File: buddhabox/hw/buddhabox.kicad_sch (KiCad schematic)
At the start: 52 parts, among them J1 Serial, J2 SWD, J3 USB_B_Micro, J4 Speaker, J5 Battery, SW1 SW_Push, SW3 SW_Push, SW4 SW_Push, U1 TPS61291DRVR, U3 RP2040, U4 PAM8302AAD, U5 W25Q32JVZPIQ, Y1 Crystal_4pin_SMD

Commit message: Updated with working board design and pictures.
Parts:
- removed D2: LED Red, LED_SMD:LED_0603_1608Metric, symbol Device:LED_Small
- removed R5: 1k, Resistor_SMD:R_0402_1005Metric, symbol Device:R
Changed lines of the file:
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@@
-    (stroke (width 0) (type default) (color 0 0 0 0))
-  )
-  (wire (pts (xy 151.13 30.48) (xy 151.13 33.02))
     (stroke (width 0) (type default) (color 0 0 0 0))
   )
@@
     (stroke (width 0) (type default) (color 0 0 0 0))
   )
-  (wire (pts (xy 151.13 38.1) (xy 151.13 39.37))
-    (stroke (width 0) (type default) (color 0 0 0 0))
-  )
   (wire (pts (xy 166.37 124.46) (xy 166.37 137.16))
     (stroke (width 0) (type default) (color 0 0 0 0))
@@
     (stroke (width 0) (type default) (color 0 0 0 0))
   )
-  (wire (pts (xy 148.59 30.48) (xy 151.13 30.48))
-    (stroke (width 0) (type default) (color 0 0 0 0))
-  )
   (wire (pts (xy 248.92 31.75) (xy 257.81 31.75))
     (stroke (width 0) (type default) (color 0 0 0 0))
@@
   )
   (wire (pts (xy 86.36 165.1) (xy 78.74 165.1))
-    (stroke (width 0) (type default) (color 0 0 0 0))
-  )
-  (wire (pts (xy 138.43 30.48) (xy 140.97 30.48))
     (stroke (width 0) (type default) (color 0 0 0 0))
   )
@@
       (effects (font (size 1.27 1.27)) hide)
     )
-    (pin "1")
-    (pin "2")
-  )
-  (symbol (lib_id "Device:R") (at 144.78 30.48 90) (unit 1)
-    (in_bom yes) (on_board yes)
-    (property "Reference" "R5" (id 0) (at 144.78 28.448 90))
-    (property "Value" "1k" (id 1) (at 144.78 30.48 90))
-    (property "Footprint" "Resistor_SMD:R_0402_1005Metric" (id 2) (at 144.78 32.258 0)
-      (effects (font (size 1.27 1.27)) hide)
-    )
-    (property "Datasheet" "" (id 3) (at 144.78 30.48 0))
     (pin "1")
     (pin "2")
@@
     (pin "1")
   )
-  (symbol (lib_id "Device:LED_Small") (at 151.13 35.56 90) (unit 1)
-    (in_bom yes) (on_board yes)
-    (property "Reference" "D2" (id 0) (at 152.908 34.3916 90)
-      (effects (font (size 1.27 1.27)) (justify right))
-    )
-    (property "Value" "LED Red" (id 1) (at 152.908 36.703 90)
-      (effects (font (size 1.27 1.27)) (justify right))
-    )
-    (property "Footprint" "LED_SMD:LED_0603_1608Metric" (id 2) (at 151.13 35.56 90)
-      (effects (font (size 1.27 1.27)) hide)
-    )
-    (property "Datasheet" "~" (id 3) (at 151.13 35.56 90)
-      (effects (font (size 1.27 1.27)) hide)
-    )
-    (pin "1")
-    (pin "2")
-  )
   (symbol (lib_id "power:GND") (at 25.4 134.62 0) (unit 1)
     (in_bom yes) (on_board yes)
@@
     (pin "1")
     (pin "2")
-  )
-  (symbol (lib_id "power:GND") (at 151.13 39.37 0) (unit 1)
-    (in_bom yes) (on_board yes)
-    (property "Reference" "#PWR012" (id 0) (at 151.13 45.72 0)
-      (effects (font (size 1.27 1.27)) hide)
-    )
-    (property "Value" "GND" (id 1) (at 151.13 43.18 0))
-    (property "Footprint" "" (id 2) (at 151.13 39.37 0))
-    (property "Datasheet" "" (id 3) (at 151.13 39.37 0))
-    (pin "1")
   )
   (symbol (lib_id "Switch:SW_Push") (at 17.78 118.11 270) (unit 1)
@@
       (reference "#PWR010") (unit 1) (value "GND") (footprint "")
     )
-    (path "/cf630c1e-095e-4ed8-96bd-413e1bdb3133"
-      (reference "#PWR012") (unit 1) (value "GND") (footprint "")
-    )
     (path "/4dd818ac-3292-4a28-a1e2-f99034e0b642"
       (reference "#PWR013") (unit 1) (value "+1V1") (footprint "")
@@
       (reference "D1") (unit 1) (value "BAT54C") (footprint "Package_TO_SOT_SMD:SOT-23")
     )
-    (path "/85bc6096-6810-4070-a31a-8493abed0b37"
-      (reference "D2") (unit 1) (value "LED Red") (footprint "LED_SMD:LED_0603_1608Metric")
-    )
     (path "/abe3b920-b697-4d1e-85f2-265143b11672"
       (reference "D3") (unit 1) (value "LED Green") (footprint "LED_SMD:LED_0603_1608Metric")
@@
       (reference "R2") (unit 1) (value "1k") (footprint "Resistor_SMD:R_0402_1005Metric")
     )
-    (path "/1e216b41-6f2d-4dc7-be4b-6f214a082fa7"
-      (reference "R5") (unit 1) (value "1k") (footprint "Resistor_SMD:R_0402_1005Metric")
-    )
     (path "/c1d41f5e-3500-4d8b-aba5-66d1af96b463"

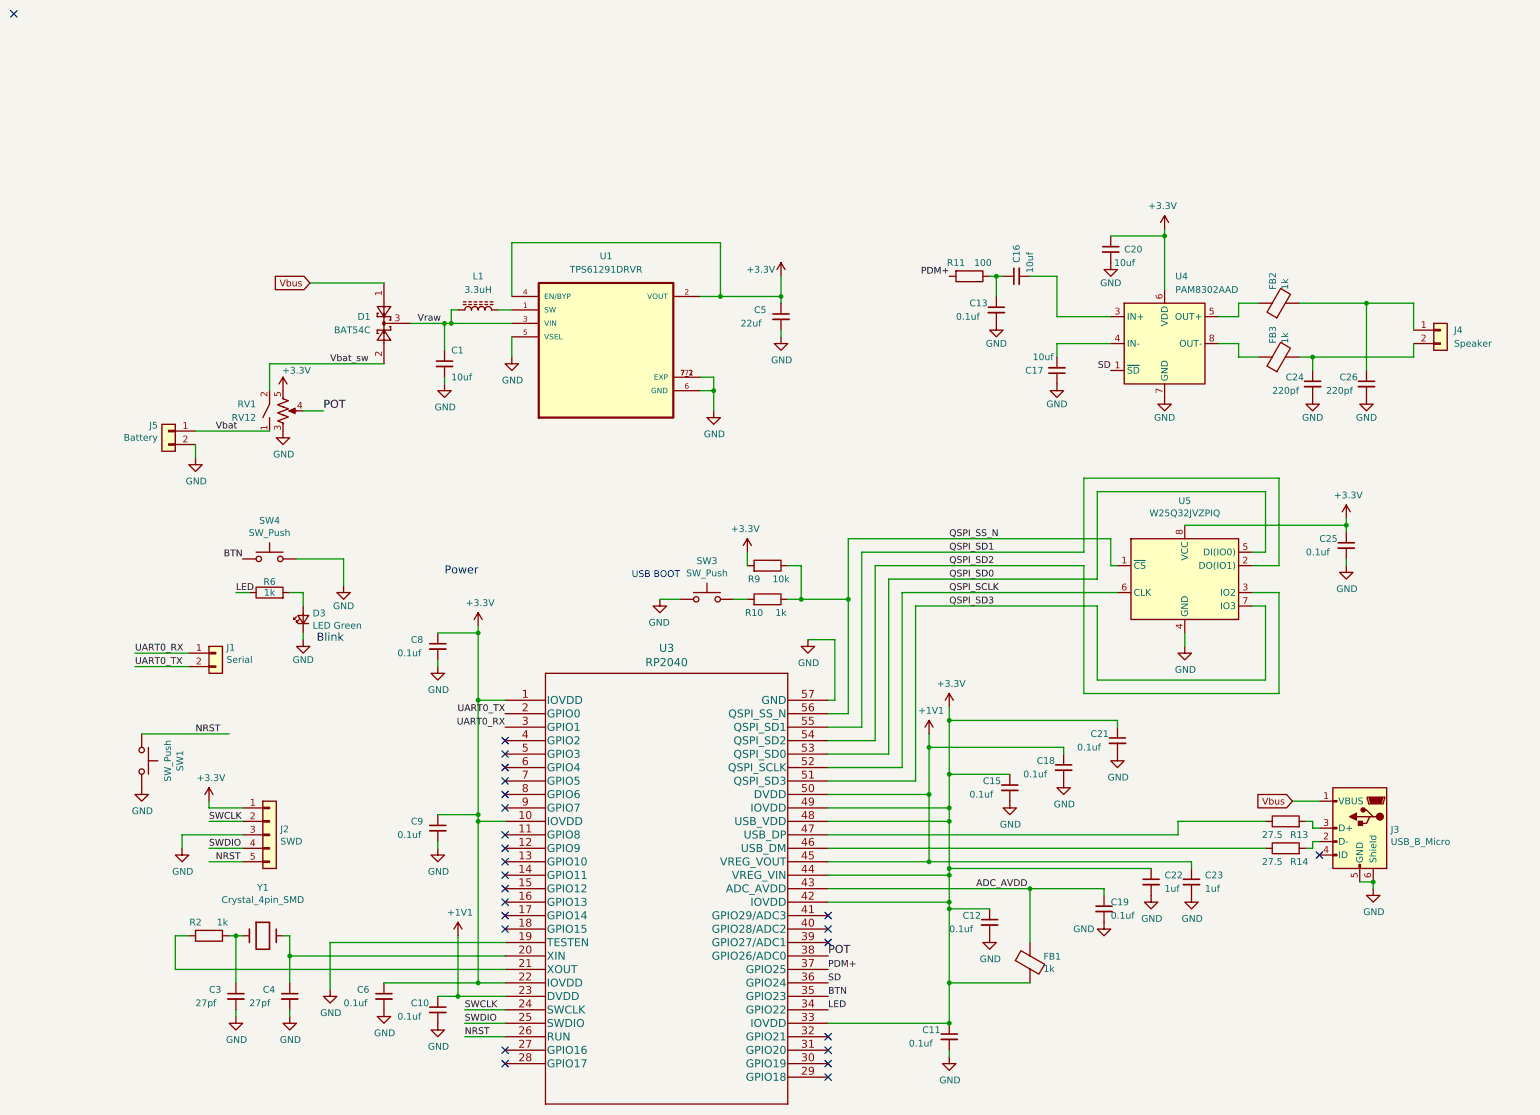
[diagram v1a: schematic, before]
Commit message: switch to i2s amp & added LDO to vbus
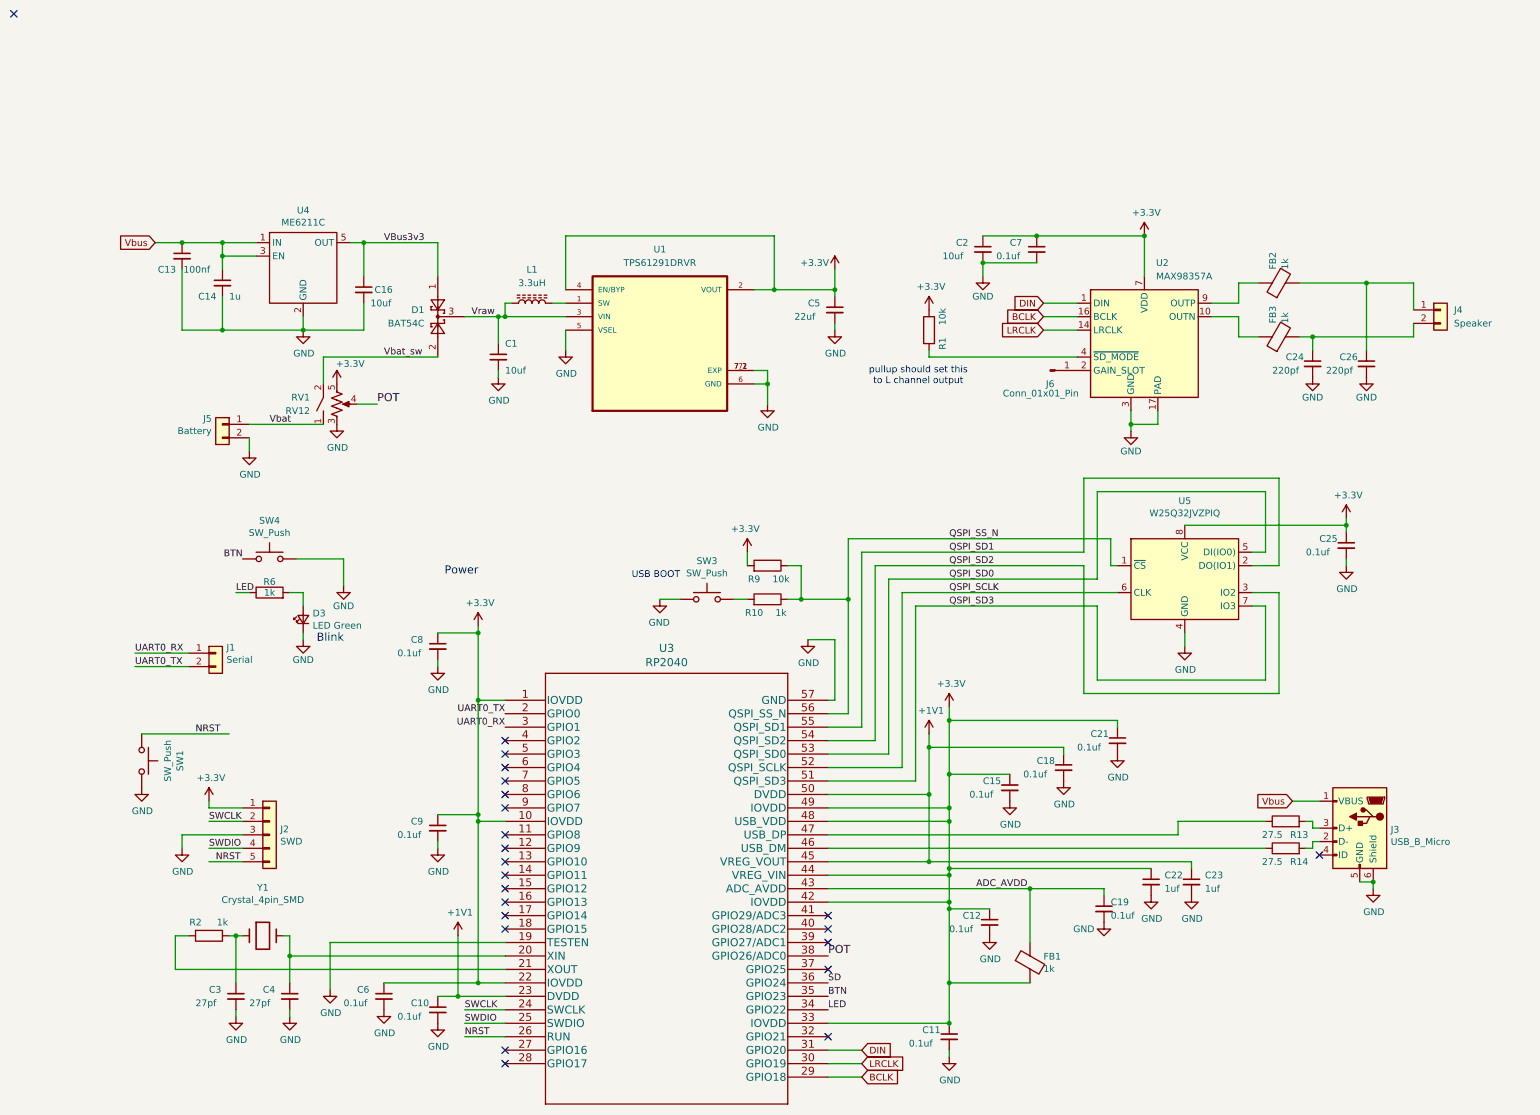
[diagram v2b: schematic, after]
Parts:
- removed C17, C20: 10uf, Capacitor_SMD:C_0805_2012Metric, symbol Device:C_Small
- removed R11: 100, Resistor_SMD:R_0402_1005Metric, symbol Device:R
- removed U4: PAM8302AAD, Package_SO:TSSOP-8_3x3mm_P0.65mm, symbol Amplifier_Audio:PAM8302AAD
- added C14: 1u, Capacitor_SMD:C_0402_1005Metric, symbol Device:C_Small
- added C2: 10uf, Capacitor_SMD:C_0402_1005Metric, symbol Device:C_Small
- added C7: 0.1uf, Capacitor_SMD:C_0402_1005Metric, symbol Device:C_Small
- added J6: Conn_01x01_Pin, symbol Connector:Conn_01x01_Pin
- added R1: 10k, Resistor_SMD:R_0402_1005Metric, symbol Device:R
- added U2: MAX98357A, Package_DFN_QFN:TQFN-16-1EP_3x3mm_P0.5mm_EP1.23x1.23mm, symbol Audio:MAX98357A
- added U4: ME6211C, Package_TO_SOT_SMD:SOT-23-5, symbol buddabox_lib:ME6211C
- C13: value 0.1uf -> 100nf
- C16: footprint Capacitor_SMD:C_0805_2012Metric -> Capacitor_SMD:C_0402_1005Metric
- U3: LCSC (none) -> C2040
- U5: LCSC (none) -> C571260
- Y1: LCSC (none) -> C9002
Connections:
- net +3.3V: now also C2.1, C7.1, R1.1, U2.7 (VDD), U2.8 (VDD)
- net GND: now also C16.2, C14.2, C2.2, C7.2, U2.11 (GND), U2.15 (GND), U2.17 (PAD), U2.3 (GND), U4.2 (GND)
- net Vbus: now also C13.1, C14.1, U4.1 (IN), U4.3 (EN); no longer D1.1
- net at FB3.1: now also U2.10 (OUTN)
- net VBus3v3: now reaches C16.1
- net VBus3v3: now also D1.1, U4.5 (OUT); no longer C13.1
- net at FB2.1: now also U2.9 (OUTP)
- net BCLK: now reaches U3.29 (GPIO18)
- net BCLK: now also U2.16 (BCLK)
- net LRCLK: now reaches U3.30 (GPIO19)
- net LRCLK: now also U2.14 (LRCLK)
- net DIN: now reaches U3.31 (GPIO20)
- net DIN: now also U2.1 (DIN)
- net PDM+: no longer names the net of U3.37 (GPIO25)
- new net: R1.2, U2.4 (~{SD_MODE})
- new net: J6.1 (Pin_1), U2.2 (GAIN_SLOT)
- no-connect marks 25 -> 23
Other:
- note added: "pullup should set this to L channel output"
- moved on the sheet: C1, C24, C26, C5, D1, FB2, FB3, J4, J5, L1, RV1, U1

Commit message: updated schematic with lcsc part numbers
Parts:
- removed C13: 100nf, Capacitor_SMD:C_0402_1005Metric, symbol Device:C_Small
- removed C14: 1u, Capacitor_SMD:C_0402_1005Metric, symbol Device:C_Small
- removed C16: 10uf, Capacitor_SMD:C_0402_1005Metric, symbol Device:C_Small
- removed J1: Serial, Connector_PinHeader_2.54mm:PinHeader_1x02_P2.54mm_Vertical, symbol Connector_Generic:Conn_01x02
- removed J3: USB_B_Micro, Connector_USB:USB_Micro-B_Amphenol_10103594-0001LF_Horizontal, symbol Connector:USB_B_Micro
- removed J6: Conn_01x01_Pin, symbol Connector:Conn_01x01_Pin
- removed L1: 3.3uH, Inductor_SMD:L_Taiyo-Yuden_MD-2020, symbol Device:L_Ferrite
- removed R13, R14: 27.5, Resistor_SMD:R_0402_1005Metric, symbol Device:R
- removed U1: TPS61291DRVR, emeb_library:SON65P200X200X80-7N, symbol emeb_library:TPS61291DRVR
- removed U4: ME6211C, Package_TO_SOT_SMD:SOT-23-5, symbol buddabox_lib:ME6211C
- added C17: 0.1uf, Capacitor_SMD:C_0402_1005Metric, symbol Device:C_Small
- added C20, C27: 10uf, Capacitor_SMD:C_0402_1005Metric, symbol Device:C_Small
- added J7: USB_C_Receptacle_USB2.0, MyLibrary:USB-C_SMD-TYPE-C-31-M-12, symbol Connector:USB_C_Receptacle_USB2.0
- added JP1: Jumper_2_Bridged, Jumper:SolderJumper-2_P1.3mm_Bridged_Pad1.0x1.5mm, symbol Jumper:Jumper_2_Bridged
- added L2: 1.5uH, Inductor_SMD:L_Coilcraft_LPS3010, symbol Device:L_Ferrite
- added R3, R4: 5.1k, Resistor_SMD:R_0402_1005Metric, symbol Device:R
- added R5, R7: 27.4, Resistor_SMD:R_0402_1005Metric, symbol Device:R
- added R8: 100k, Resistor_SMD:R_0805_2012Metric, symbol Device:R
- added U6: TPS63031DSK, Package_SON:WSON-10-1EP_2.5x2.5mm_P0.5mm_EP1.2x2mm, symbol Regulator_Switching:TPS63031DSK
- C1: footprint Capacitor_SMD:C_0805_2012Metric -> Capacitor_SMD:C_0402_1005Metric; LCSC (none) -> C15525
- C10, C11, C12, C15, C18, C19, C21, C25, C6, C7, C8, C9: LCSC (none) -> C1525
- C2: LCSC (none) -> C15525
- C22, C23: LCSC (none) -> C52923
- C24, C26: LCSC (none) -> C1530
- C3, C4: value 27pf -> 30pf; footprint Capacitor_SMD:C_0402_1005Metric -> Capacitor_SMD:C_0603_1608Metric; LCSC (none) -> C1658
- C5: value 22uf -> 10uf; footprint Capacitor_SMD:C_1210_3225Metric -> Capacitor_SMD:C_0402_1005Metric; LCSC (none) -> C15525
- D1: LCSC (none) -> C556168
- D3: LCSC (none) -> C2286
- FB1, FB2, FB3: value 1k -> 600@100mhz; footprint Inductor_SMD:L_0402_1005Metric -> Inductor_SMD:L_0603_1608Metric; LCSC (none) -> C1002
- J2: value SWD -> PICOPROBE
- R1, R9: LCSC (none) -> C25744
- R10, R2, R6: LCSC (none) -> C11702
- SW1, SW3: LCSC (none) -> C221675
- SW4: value SW_Push -> SW_PushSide; LCSC (none) -> DNP
- U2: LCSC (none) -> C910544
- U5: value W25Q32JVZPIQ -> W25Q64JVZPIQ; LCSC C571260 -> C2940197
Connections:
- net VBus3v3 is gone; now on net Vbus: D1.1
- net +3.3V: now also C20.1, C27.1, JP1.1 (A), U6.1 (VOUT), U6.10 (FB); no longer C5.1, J2.1 (Pin_1)
- net GND: now also J2.1 (Pin_1), C17.2, C20.2, C27.2, J7.A1 (GND), J7.A12 (GND), J7.B1 (GND), J7.B12 (GND), J7.S1 (SHIELD), R3.1, R4.1, U6.11 (PGND), U6.3 (PGND), U6.9 (GND); no longer J2.3 (Pin_3)
- net NRST: no longer J2.5 (Pin_5)
- net SWDIO: now also J2.3 (Pin_3); no longer J2.4 (Pin_4)
- net UART0_RX: now also J2.4 (Pin_4)
- net UART0_TX: now also J2.5 (Pin_5)
- net Vbus: now also C5.1, J7.A4 (VBUS), J7.A9 (VBUS), J7.B4 (VBUS), J7.B9 (VBUS)
- net Vraw: now also U6.5 (VIN)
- net at U2.2 (GAIN_SLOT): now also R8.2
- net usb_D-: now reaches U3.46 (USB_DM)
- net usb_D-: now also R5.1
- net usb_D+: now reaches U3.47 (USB_DP)
- net usb_D+: now also R7.1
- new net: L2.1, U6.2 (L2)
- new net: L2.2, U6.4 (L1)
- new net: J7.B5 (CC2), R3.2
- new net: J7.A7 (D-), J7.B7 (D-), R5.2
- new net: J7.A5 (CC1), R4.2
- new net: J7.A6 (D+), J7.B6 (D+), R7.2
- new net: C17.1, U6.6 (EN), U6.7 (PS/SYNC), U6.8 (VINA)
- new net: JP1.2 (B), R8.1
- no-connect marks 23 -> 24
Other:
- note removed: "pullup should set this to L channel output"
- moved on the sheet: C1
